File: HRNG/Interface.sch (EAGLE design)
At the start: 16 parts, among them IC1 LM358N, IC2 FT232RL, J1 PIC_ICSP_6_PINPOLAR_LOCK, J2 USB_MINI-B_SMT

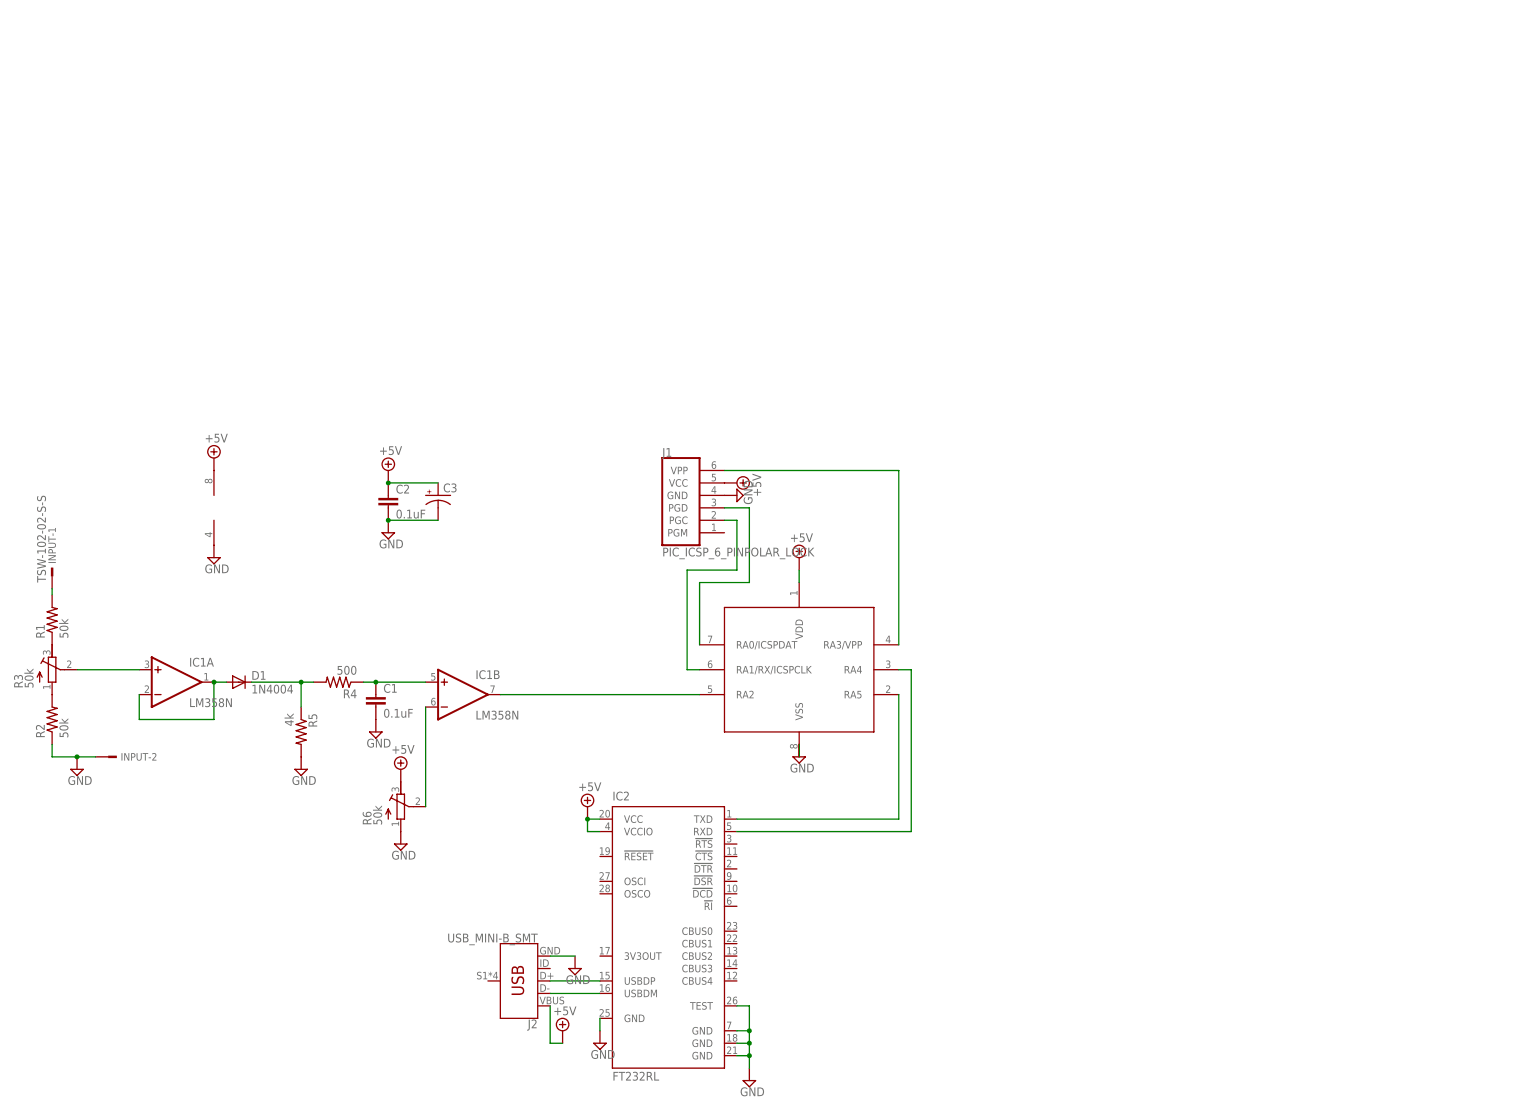
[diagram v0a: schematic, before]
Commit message: Encrypter work
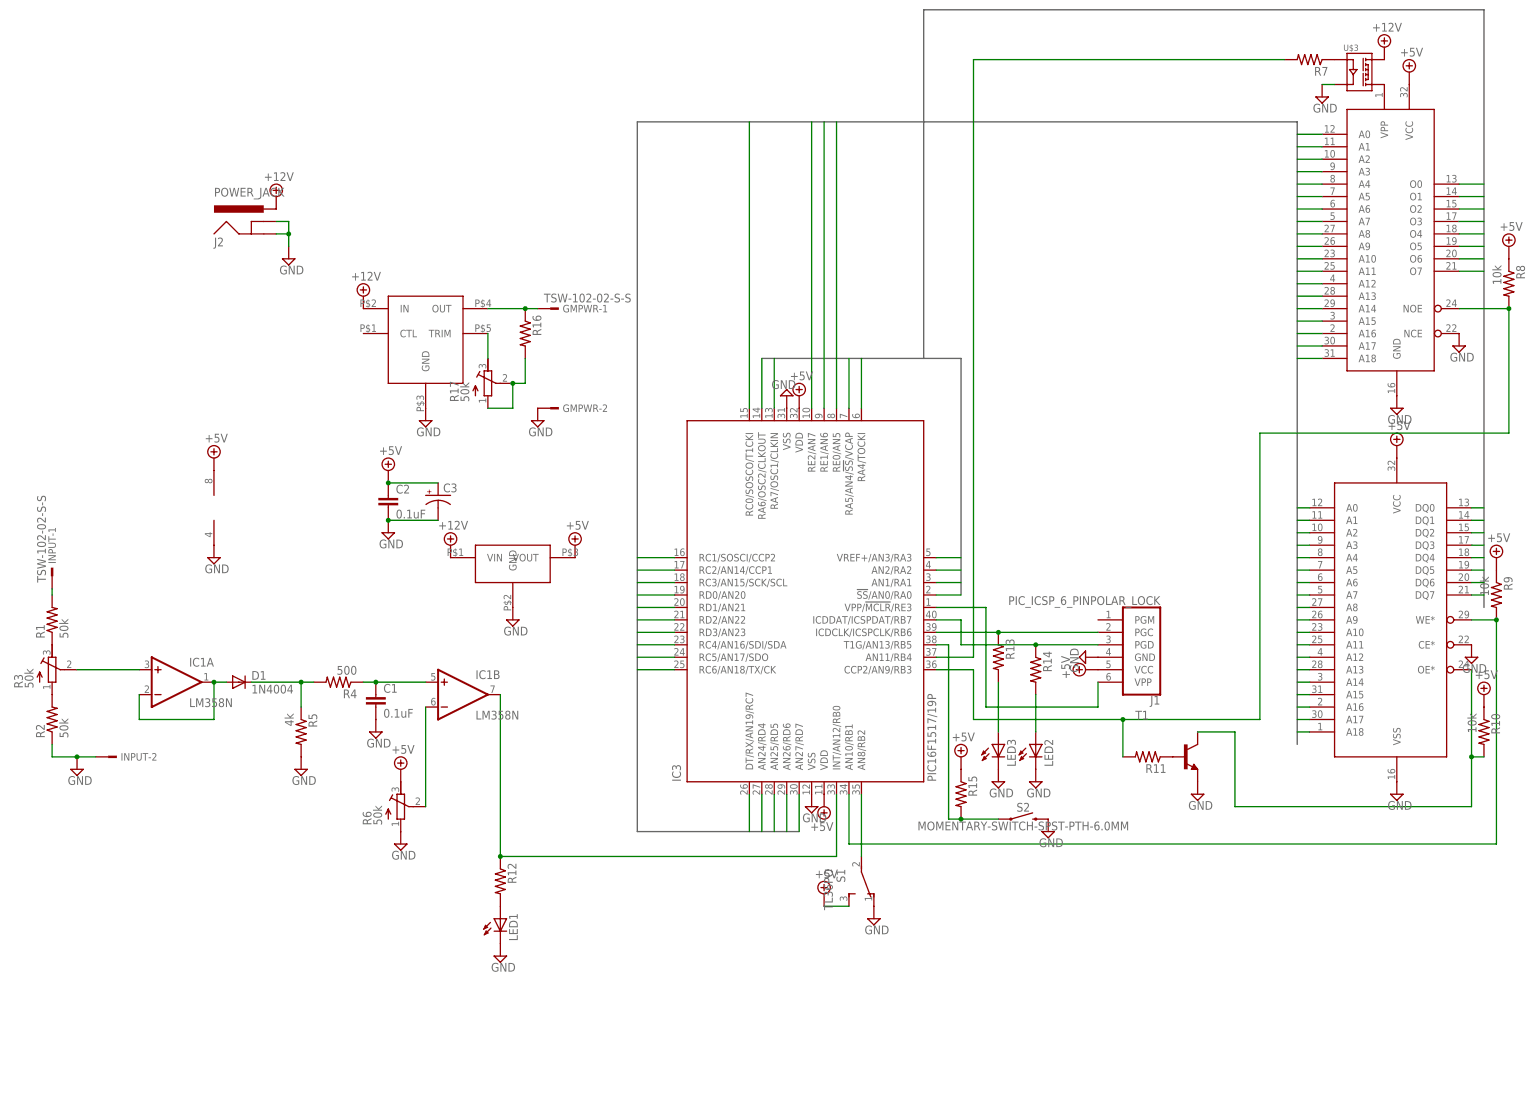
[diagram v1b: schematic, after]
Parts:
- removed IC2: FT232RL, ftdichip:FT232RL
- added GMPWR: TSW-102-02-S-S, con-samtec:TSW-102-02-S-S
- added IC3: PIC16F1517/19P, microchip:PIC16F1517/19P
- added LED1, LED2, LED3: (no value), led:LED3MM
- added R10, R8, R9: 10k, resistor:R-US_0204/2V
- added R11, R12, R13, R14, R15, R16, R7: (no value), resistor:R-US_0204/2V
- added R17: 50k, resistor:R-TRIMM3296W
- added S1: TL36PO, switch:TL36PO
- added S2: MOMENTARY-SWITCH-SPST-PTH-6.0MM, SparkFun-Switches:MOMENTARY-SWITCH-SPST-PTH-6.0MM
- added T1: (no value), transistor:MPS2222A-NPN-TO92-CBE
- added U$2: AS6C4008, Football:AS6C4008
- added U$3: CPC1008N, JSB2:CPC1008N
- added U$4: OKR-T/1.5-W12-C, Football:OKR-T
- added U$5: OKI-78SR-5/1.5-W36-C, JSB2:OKI-78SR-5/1.5-W36-C
- J2: value USB_MINI-B_SMT -> POWER_JACK; device SparkFun-Connectors:USB_MINI-B_SMT -> SparkFun-Connectors:POWER_JACK
- U$1: value PIC16F18313 -> AT27C040; device PIC16:PIC16F18313 -> Football:AT27C040
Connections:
- new net +12V: J2.PWR, U$3.DC@1, U$4.IN, U$5.VIN
- new net A0: IC3.RC0/SOSCO/T1CKI, U$1.A0, U$2.A0
- new net A1: IC3.RC1/SOSCI/CCP2, U$1.A1, U$2.A1
- new net A10: IC3.RD2/AN22, U$1.A10, U$2.A10
- new net A11: IC3.RD3/AN23, U$1.A11, U$2.A11
- new net A12: IC3.AN24/RD4, U$1.A12, U$2.A12
- new net A13: IC3.AN25/RD5, U$1.A13, U$2.A13
- new net A14: IC3.AN26/RD6, U$1.A14, U$2.A14
- new net A15: IC3.AN27/RD7, U$1.A15, U$2.A15
- new net A16: IC3.RE0/AN5, U$1.A16, U$2.A16
- new net A17: IC3.RE1/AN6, U$1.A17, U$2.A17
- new net A18: IC3.RE2/AN7, U$1.A18, U$2.A18
- new net A2: IC3.RC2/AN14/CCP1, U$1.A2, U$2.A2
- new net A3: IC3.RC3/AN15/SCK/SCL, U$1.A3, U$2.A3
- new net A4: IC3.RC4/AN16/SDI/SDA, U$1.A4, U$2.A4
- new net A5: IC3.RC5/AN17/SDO, U$1.A5, U$2.A5
- new net A6: IC3.RC6/AN18/TX/CK, U$1.A6, U$2.A6
- new net A7: IC3.DT/RX/AN19/RC7, U$1.A7, U$2.A7
- new net A8: IC3.RD0/AN20, U$1.A8, U$2.A8
- new net A9: IC3.RD1/AN21, U$1.A9, U$2.A9
- new net D0: IC3.!SS!/AN0/RA0, U$1.O0, U$2.DQ0
- new net D1: IC3.AN1/RA1, U$1.O1, U$2.DQ1
- new net D2: IC3.AN2/RA2, U$1.O2, U$2.DQ2
- new net D3: IC3.VREF+/AN3/RA3, U$1.O3, U$2.DQ3
- new net D4: IC3.RA4/TOCKI, U$1.O4, U$2.DQ4
- new net D5: IC3.RA5/AN4/!SS!/VCAP, U$1.O5, U$2.DQ5
- new net D6: IC3.RA6/OSC2/CLKOUT, U$1.O6, U$2.DQ6
- new net D7: IC3.RA7/OSC1/CLKIN, U$1.O7, U$2.DQ7
- new net N$15: IC3.VPP/!MCLR!/RE3, J1.VPP
- new net N$16: U$1.VPP, U$3.DC@2
- new net N$19: R10.2, T1.C, U$2.OE*
- new net N$20: LED1.A, R12.2
- new net N$21: IC3.AN8/RB2, S1.P
- new net N$22: LED2.A, R14.2
- new net N$23: LED3.A, R13.2
- new net N$24: IC3.T1G/AN13/RB5, R15.2, S2.1
- new net N$25: GMPWR-1.1, R16.1, U$4.OUT
- new net N$26: R17.E, U$4.TRIM
- new net N$27: R16.2, R17.A, R17.S
- net +5V: now also IC3.VDD, IC3.VDD@1, R10.1, R15.1, R8.1, R9.1, S1.S, U$1.VCC, U$2.VCC, U$5.VOUT; no longer IC2.VCC, IC2.VCCIO, J2.VBUS, U$1.VDD
- net GND: now also GMPWR-2.1, IC3.VSS, IC3.VSS@1, J2.GNDBREAK, LED1.C, LED2.C, LED3.C, S1.O, S2.2, T1.E, U$1.GND, U$1.NCE, U$2.CE*, U$2.VSS, U$3.IN-, U$4.GND, U$5.GND; no longer IC2.GND, IC2.GND@1, IC2.GND@2, IC2.GND@A, IC2.TEST, U$1.VSS
- net N$10: now also IC3.ICDDAT/ICSPDAT/RB7, J1.PGD, R14.1; no longer J1.PGC, U$1.RA1/RX/ICSPCLK
- net N$11: now also IC3.AN10/RB1, R9.2, U$2.WE*; no longer J1.VPP, U$1.RA3/VPP
- net N$12: now also R11.1, T1.B; no longer IC1B.OUT, U$1.RA2
- net N$13: now also IC3.CCP2/AN9/RB3, R11.2, R8.2, U$1.NOE; no longer IC2.USBDP, J2.D+
- net N$14: now also IC1B.OUT, IC3.INT/AN12/RB0, R12.1; no longer IC2.USBDM, J2.D-
- net N$17: now also R7.1, U$3.IN+; no longer IC2.TXD, U$1.RA5
- net N$18: now also IC3.AN11/RB4, R7.2; no longer IC2.RXD, U$1.RA4
- net N$9: now also IC3.ICDCLK/ICSPCLK/RB6, J1.PGC, R13.1; no longer J1.PGD, U$1.RA0/ICSPDAT
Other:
- moved on the sheet: J1
